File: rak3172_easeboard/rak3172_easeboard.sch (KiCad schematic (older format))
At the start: 40 parts, among them J1 Conn_Coaxial, J2 USB_C_Receptacle, SW1 SW_Push, SW2 SW_Push, U1 RAK3172, U2 FT232RL, U3 SPX3819

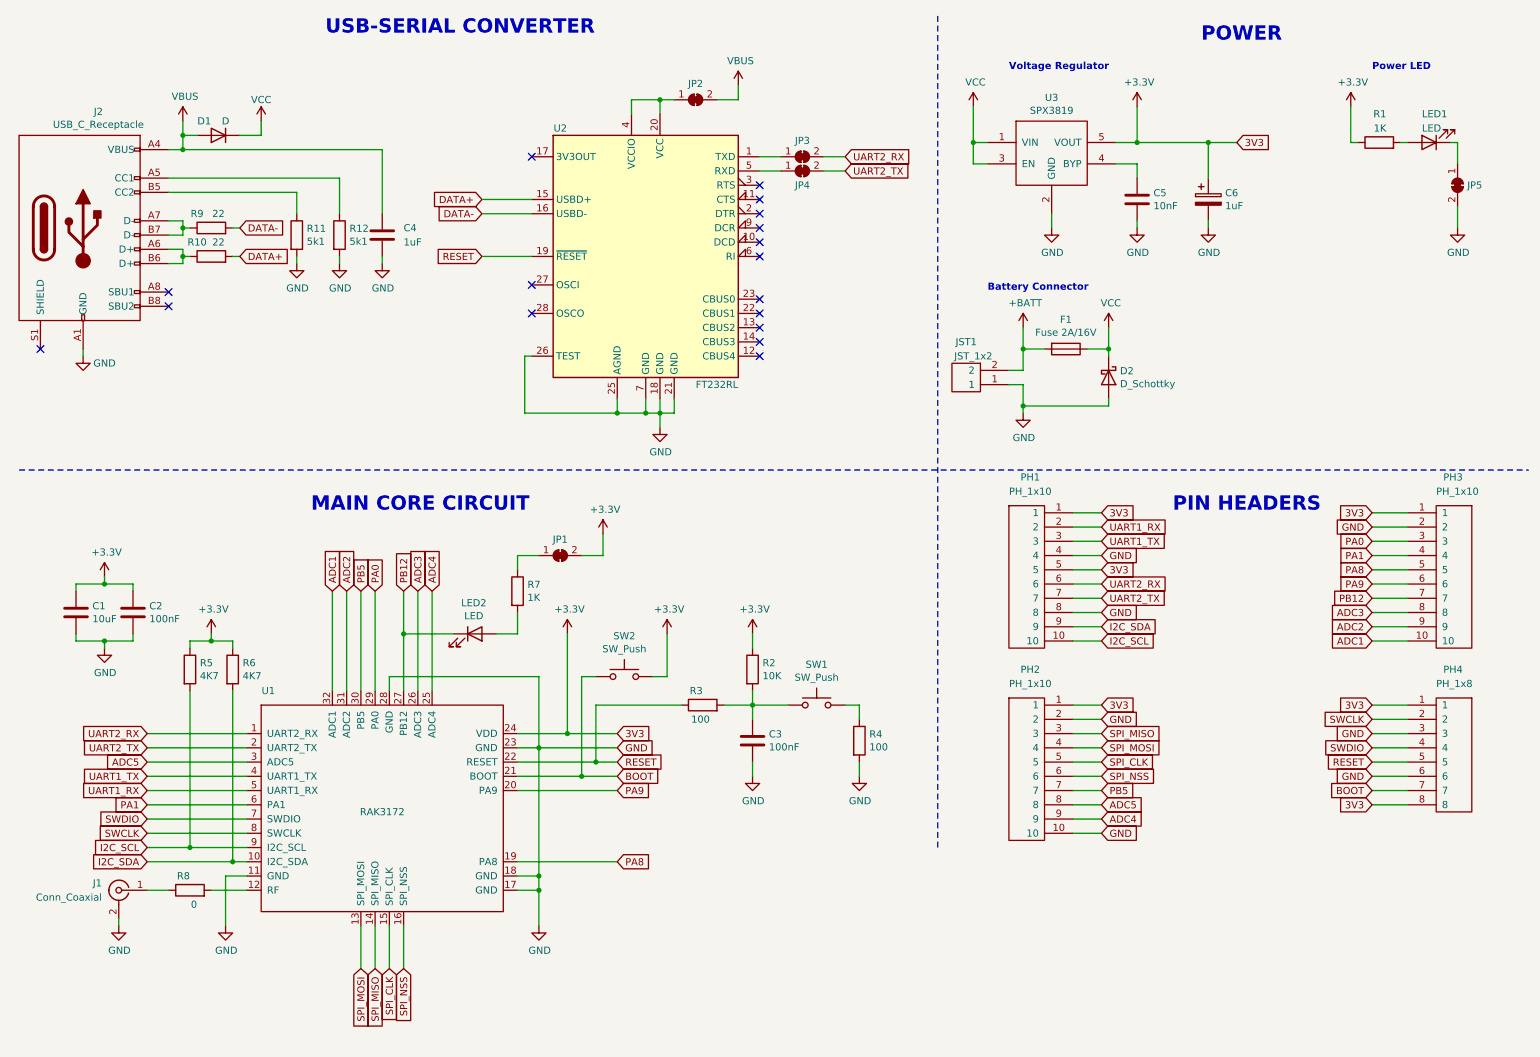
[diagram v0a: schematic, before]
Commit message: Update antenna trace. Added BOM
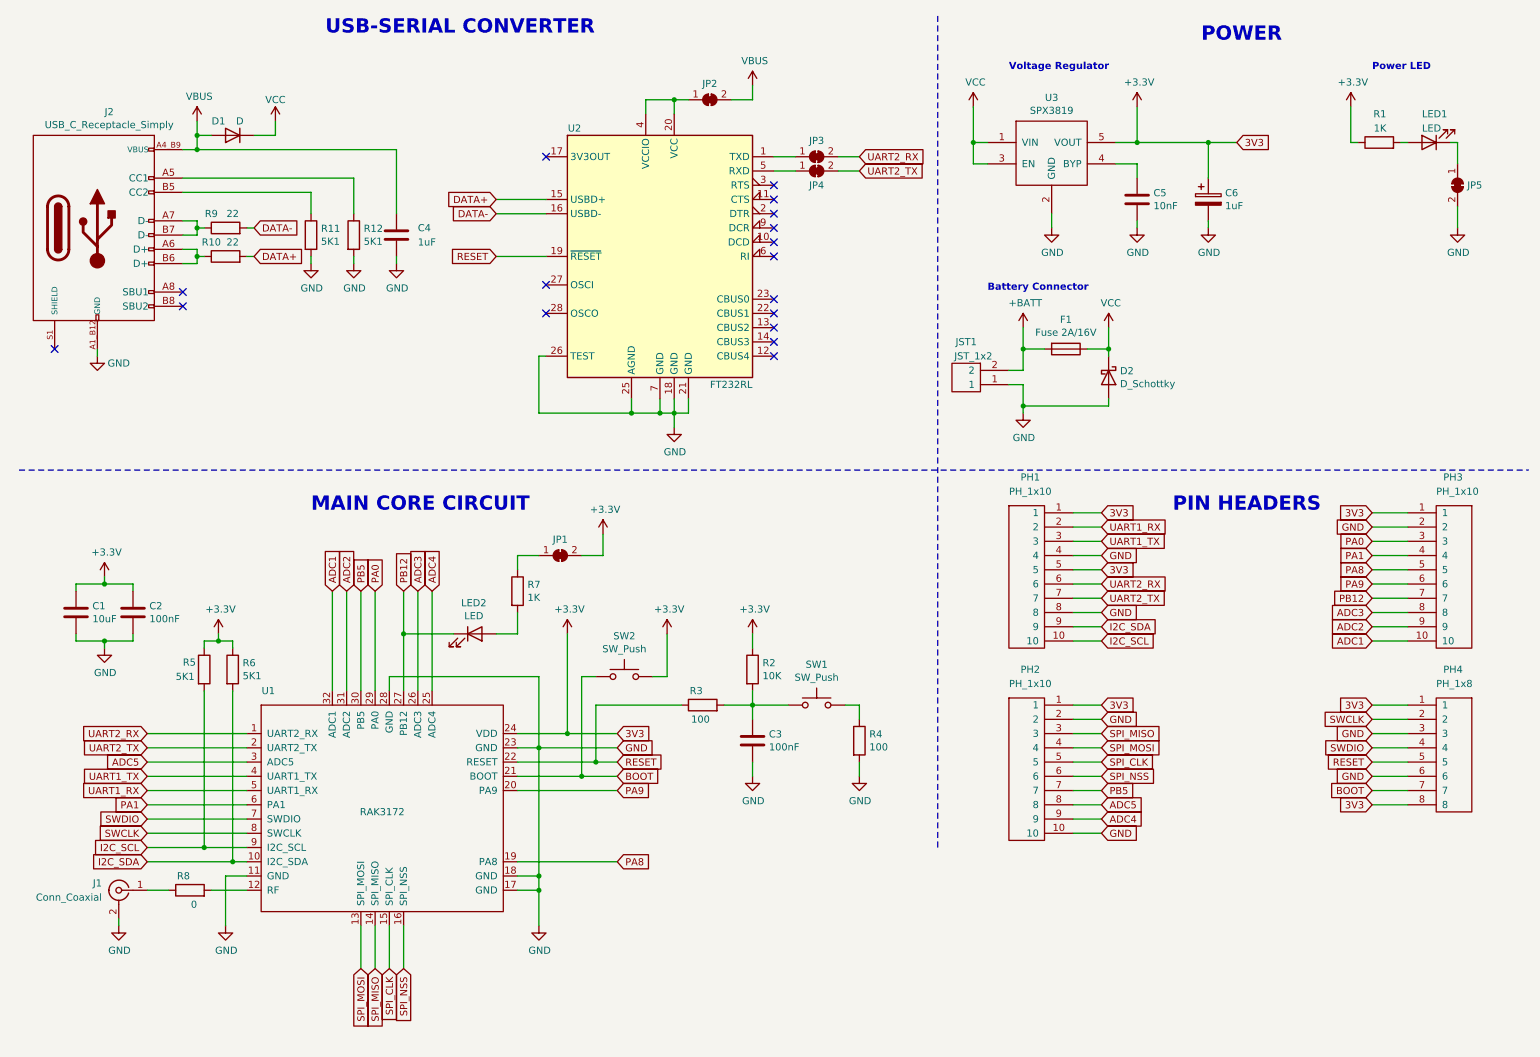
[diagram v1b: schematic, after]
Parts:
- removed J2: USB_C_Receptacle, rak3172_easeboard:USB_C_Receptacle_HRO_TYPE-C-31-M-12, symbol rak3172_easeboard:USB_C_Receptacle
- added J2: USB_C_Receptacle_Simply, rak3172_easeboard:USB_C_Receptacle_12, symbol rak3172_easeboard:USB_C_Receptacle_Simply
- C1: Last Seen Price (eur) (none) -> 0.14; Mouser (none) -> https://www.mouser.es/ProductDetail/Samsung-Electro-Mechani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
- C2, C3: Last Seen Price (eur) (none) -> 0.09; Mouser (none) -> https://www.mouser.es/ProductDetail/KEMET/C0805C104M5RACTU?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
- C4: Last Seen Price (eur) (none) -> 0.09; Mouser (none) -> https://www.mouser.es/ProductDetail/KEMET/C0805C105Z4VACTU?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
- C5: Last Seen Price (eur) (none) -> 0.09; Mouser (none) -> https://www.mouser.es/ProductDetail/KEMET/C0805C103J5RACTU?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
- C6: footprint rak3172_easeboard:C_1206_3216Metric_Pad1.33x1.80mm_HandSolder -> rak3172_easeboard:C_0805_2012Metric_Pad1.18x1.45mm_HandSolder; Last Seen Price (eur) (none) -> 0.09; Mouser (none) -> https://www.mouser.es/ProductDetail/KEMET/C0805C105Z4VACTU?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
- D1: Last Seen Price (eur) (none) -> 0.29; Mouser (none) -> https://www.mouser.es/ProductDetail/Taiwan-Semiconductor/TS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
- D2: Last Seen Price (eur) (none) -> 0.32; Mouser (none) -> https://www.mouser.es/ProductDetail/Kyocera-AVX/SD0805S020S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
- F1: Last Seen Price (eur) (none) -> 0.42; Mouser (none) -> https://www.mouser.es/ProductDetail/Littelfuse/1812L150-16D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
- JST1: Last Seen Price (eur) (none) -> 0.64; Mouser (none) -> https://www.mouser.es/ProductDetail/Adafruit/1769?qs=sGAEpi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
- LED1, LED2: Last Seen Price (eur) (none) -> 0.15; Mouser (none) -> https://www.mouser.es/ProductDetail/Wurth-Elektronik/150080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
- R1, R7: Last Seen Price (eur) (none) -> 0.09; Mouser (none) -> https://www.mouser.es/ProductDetail/Susumu/RR1220P-102-D?qs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
- R10, R9: Last Seen Price (eur) (none) -> 0.09; Mouser (none) -> https://www.mouser.es/ProductDetail/Susumu/RR1220Q-220-D?qs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
- R11, R12: value 5k1 -> 5K1; Last Seen Price (eur) (none) -> 0.09; Mouser (none) -> https://www.mouser.es/ProductDetail/Panasonic/ERA-6AED512V?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
- R2: Last Seen Price (eur) (none) -> 0.09; Mouser (none) -> https://www.mouser.es/ProductDetail/Susumu/RR1220P-103-D?qs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
- R3, R4: Last Seen Price (eur) (none) -> 0.09; Mouser (none) -> https://www.mouser.es/ProductDetail/Susumu/RR1220P-101-D?qs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
- R5, R6: value 4K7 -> 5K1; Last Seen Price (eur) (none) -> 0.09; Mouser (none) -> https://www.mouser.es/ProductDetail/Panasonic/ERA-6AED512V?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
- SW1, SW2: Last Seen Price (eur) (none) -> 0.21; Mouser (none) -> https://www.mouser.es/ProductDetail/Schurter/13019318?qs=tG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
- U1: Last Seen Price (eur) (none) -> 5.15; Mouser (none) -> https://store.rakwireless.com/products/wisduo-lpwan-module-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
- U3: Last Seen Price (eur) (none) -> 0.47; Mouser (none) -> https://www.mouser.es/ProductDetail/MaxLinear/SPX3819M5-L-3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
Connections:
- net GND: now also J2.A1_B12 (GND), J2.B1_A12 (GND)
- net VBUS: now also J2.A4_B9 (VBUS), J2.B4_A9 (VBUS)
- net at R12.1: now also J2.A5 (CC1)
- net at R10.1: now also J2.A6 (D+), J2.B6 (D+)
- net at R9.1: now also J2.A7 (D-), J2.B7 (D-)
- net at R11.1: now also J2.B5 (CC2)
- new net SHIELD: J2.S1 (SHIELD), J2.S2 (SHIELD), J2.S3 (SHIELD), J2.S4 (SHIELD)
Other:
- moved on the sheet: C4, D1, JP2, JP3, JP4, R10, R11, R12, R5, R9, U2

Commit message: UART serie protection resistors
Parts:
- added R13, R14, R15, R16: 22, rak3172_easeboard:R_0805_2012Metric_Pad1.20x1.40mm_HandSolder, symbol rak3172_easeboard:R
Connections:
- net UART1_RX: now also R16.1; no longer U1.5 (UART1_RX)
- net UART1_TX: now also R15.1; no longer U1.4 (UART1_TX)
- net UART2_RX: now also R13.1; no longer U1.1 (UART2_RX)
- net UART2_TX: now also R14.1; no longer U1.2 (UART2_TX)
- new net: R13.2, U1.1 (UART2_RX)
- new net: R14.2, U1.2 (UART2_TX)
- new net: R15.2, U1.4 (UART1_TX)
- new net: R16.2, U1.5 (UART1_RX)
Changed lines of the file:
@@
 Wire Wire Line
 	2150 6100 1450 6100
-$Comp
-L rak3172_easeboard:RAK3172 U1
-U 1 1 6153A147
-P 3100 6150
-F 0 "U1" H 2300 7000 50  0000 C CNN
-F 1 "RAK3172" H 3100 6150 50  0000 C CNN
-F 2 "rak3172_easeboard:RAK3172" H 2250 5400 50  0001 C CNN
-F 3 "https://docs.rakwireless.com/Product-Categories/WisDuo/RAK3172-Module/Datasheet" H 2300 7000 50  0001 C CNN
-F 4 "5.15" H 3100 6150 50  0001 C CNN "Last Seen Price (eur)"
-F 5 "https://store.rakwireless.com/products/wisduo-lpwan-module-rak3172?utm_source=rak3172landingpage&utm_medium=header&utm_campaign=RAKwireless&variant=40014759329990" H 3100 6150 50  0001 C CNN "Mouser"
-	1    3100 6150
-	1    0    0    -1
-$EndComp
 Wire Wire Line
 	1450 6500 2050 6500
@@
 Text GLabel 1450 6400 0    50   Input ~ 0
 I2C_SCL
-Text GLabel 1450 5900 0    50   Input ~ 0
-UART1_TX
-Text GLabel 1450 5800 0    50   Input ~ 0
-ADC5
 Text GLabel 1450 6100 0    50   Input ~ 0
 PA1
-Text GLabel 1450 6000 0    50   Input ~ 0
-UART1_RX
 Text GLabel 1450 6300 0    50   Input ~ 0
 SWCLK
@@
 	1    0    0    -1
 $EndComp
-Text GLabel 1450 5600 0    50   Input ~ 0
-UART2_RX
-Text GLabel 1450 5700 0    50   Input ~ 0
-UART2_TX
 Wire Wire Line
 	6300 1650 6450 1650
@@
 Wire Wire Line
 	5700 5400 5500 5400
-Wire Wire Line
-	2150 5600 1450 5600
-Wire Wire Line
-	1450 5700 2150 5700
-Wire Wire Line
-	2150 5800 1450 5800
-Wire Wire Line
-	1450 5900 2150 5900
-Wire Wire Line
-	2150 6000 1450 6000
+$Comp
+L rak3172_easeboard:RAK3172 U1
+U 1 1 6153A147
+P 3100 6150
+F 0 "U1" H 2300 7000 50  0000 C CNN
+F 1 "RAK3172" H 3100 6150 50  0000 C CNN
+F 2 "rak3172_easeboard:RAK3172" H 2250 5400 50  0001 C CNN
+F 3 "https://docs.rakwireless.com/Product-Categories/WisDuo/RAK3172-Module/Datasheet" H 2300 7000 50  0001 C CNN
+F 4 "5.15" H 3100 6150 50  0001 C CNN "Last Seen Price (eur)"
+F 5 "https://store.rakwireless.com/products/wisduo-lpwan-module-rak3172?utm_source=rak3172landingpage&utm_medium=header&utm_campaign=RAKwireless&variant=40014759329990" H 3100 6150 50  0001 C CNN "Mouser"
+	1    3100 6150
+	1    0    0    -1
+$EndComp
+Wire Wire Line
+	2150 6000 1800 6000
+Wire Wire Line
+	1800 5900 2150 5900
+Wire Wire Line
+	1800 5600 2150 5600
+Wire Wire Line
+	2150 5700 1800 5700
+Wire Wire Line
+	1450 5800 2150 5800
+Text GLabel 1450 5800 0    50   Input ~ 0
+ADC5
+Text GLabel 1450 5600 0    50   Input ~ 0
+UART2_RX
+Text GLabel 1450 5700 0    50   Input ~ 0
+UART2_TX
+Wire Wire Line
+	1450 5600 1500 5600
+Wire Wire Line
+	1500 5700 1450 5700
+$Comp
+L rak3172_easeboard:R R13
+U 1 1 61984AB7
+P 1650 5600
+F 0 "R13" V 1850 5700 50  0000 C CNN
+F 1 "22" V 1850 5550 50  0000 C CNN
+F 2 "rak3172_easeboard:R_0805_2012Metric_Pad1.20x1.40mm_HandSolder" V 1580 5600 50  0001 C CNN
+F 3 "https://www.mouser.es/datasheet/2/392/susumu_RR_Data_Sheet-1206438.pdf" H 1650 5600 50  0001 C CNN
+F 4 "0.09" H 1650 5600 50  0001 C CNN "Last Seen Price (eur)"
+F 5 "https://www.mouser.es/ProductDetail/Susumu/RR1220Q-220-D?qs=U7dmUkNviFsL4com4sXnaQ%3D%3D" H 1650 5600 50  0001 C CNN "Mouser"
+	1    1650 5600
+	0    -1   -1   0
+$EndComp
+$Comp
+L rak3172_easeboard:R R14
+U 1 1 61984AAF
+P 1650 5700
+F 0 "R14" V 1850 5800 50  0000 C CNN
+F 1 "22" V 1850 5650 50  0000 C CNN
+F 2 "rak3172_easeboard:R_0805_2012Metric_Pad1.20x1.40mm_HandSolder" V 1580 5700 50  0001 C CNN
+F 3 "https://www.mouser.es/datasheet/2/392/susumu_RR_Data_Sheet-1206438.pdf" H 1650 5700 50  0001 C CNN
+F 4 "0.09" H 1650 5700 50  0001 C CNN "Last Seen Price (eur)"
+F 5 "https://www.mouser.es/ProductDetail/Susumu/RR1220Q-220-D?qs=U7dmUkNviFsL4com4sXnaQ%3D%3D" H 1650 5700 50  0001 C CNN "Mouser"
+	1    1650 5700
+	0    -1   -1   0
+$EndComp
+Wire Wire Line
+	1500 5900 1450 5900
+Wire Wire Line
+	1450 6000 1500 6000
+$Comp
+L rak3172_easeboard:R R16
+U 1 1 619D2833
+P 1650 6000
+F 0 "R16" V 1650 6100 50  0000 C CNN
+F 1 "22" V 1650 5950 50  0000 C CNN
+F 2 "rak3172_easeboard:R_0805_2012Metric_Pad1.20x1.40mm_HandSolder" V 1580 6000 50  0001 C CNN
+F 3 "https://www.mouser.es/datasheet/2/392/susumu_RR_Data_Sheet-1206438.pdf" H 1650 6000 50  0001 C CNN
+F 4 "0.09" H 1650 6000 50  0001 C CNN "Last Seen Price (eur)"
+F 5 "https://www.mouser.es/ProductDetail/Susumu/RR1220Q-220-D?qs=U7dmUkNviFsL4com4sXnaQ%3D%3D" H 1650 6000 50  0001 C CNN "Mouser"
+	1    1650 6000
+	0    -1   -1   0
+$EndComp
+Text GLabel 1450 6000 0    50   Input ~ 0
+UART1_RX
+Text GLabel 1450 5900 0    50   Input ~ 0
+UART1_TX
+$Comp
+L rak3172_easeboard:R R15
+U 1 1 619D283B
+P 1650 5900
+F 0 "R15" V 1650 6000 50  0000 C CNN
+F 1 "22" V 1650 5850 50  0000 C CNN
+F 2 "rak3172_easeboard:R_0805_2012Metric_Pad1.20x1.40mm_HandSolder" V 1580 5900 50  0001 C CNN
+F 3 "https://www.mouser.es/datasheet/2/392/susumu_RR_Data_Sheet-1206438.pdf" H 1650 5900 50  0001 C CNN
+F 4 "0.09" H 1650 5900 50  0001 C CNN "Last Seen Price (eur)"
+F 5 "https://www.mouser.es/ProductDetail/Susumu/RR1220Q-220-D?qs=U7dmUkNviFsL4com4sXnaQ%3D%3D" H 1650 5900 50  0001 C CNN "Mouser"
+	1    1650 5900
+	0    -1   -1   0
+$EndComp
 $EndSCHEMATC

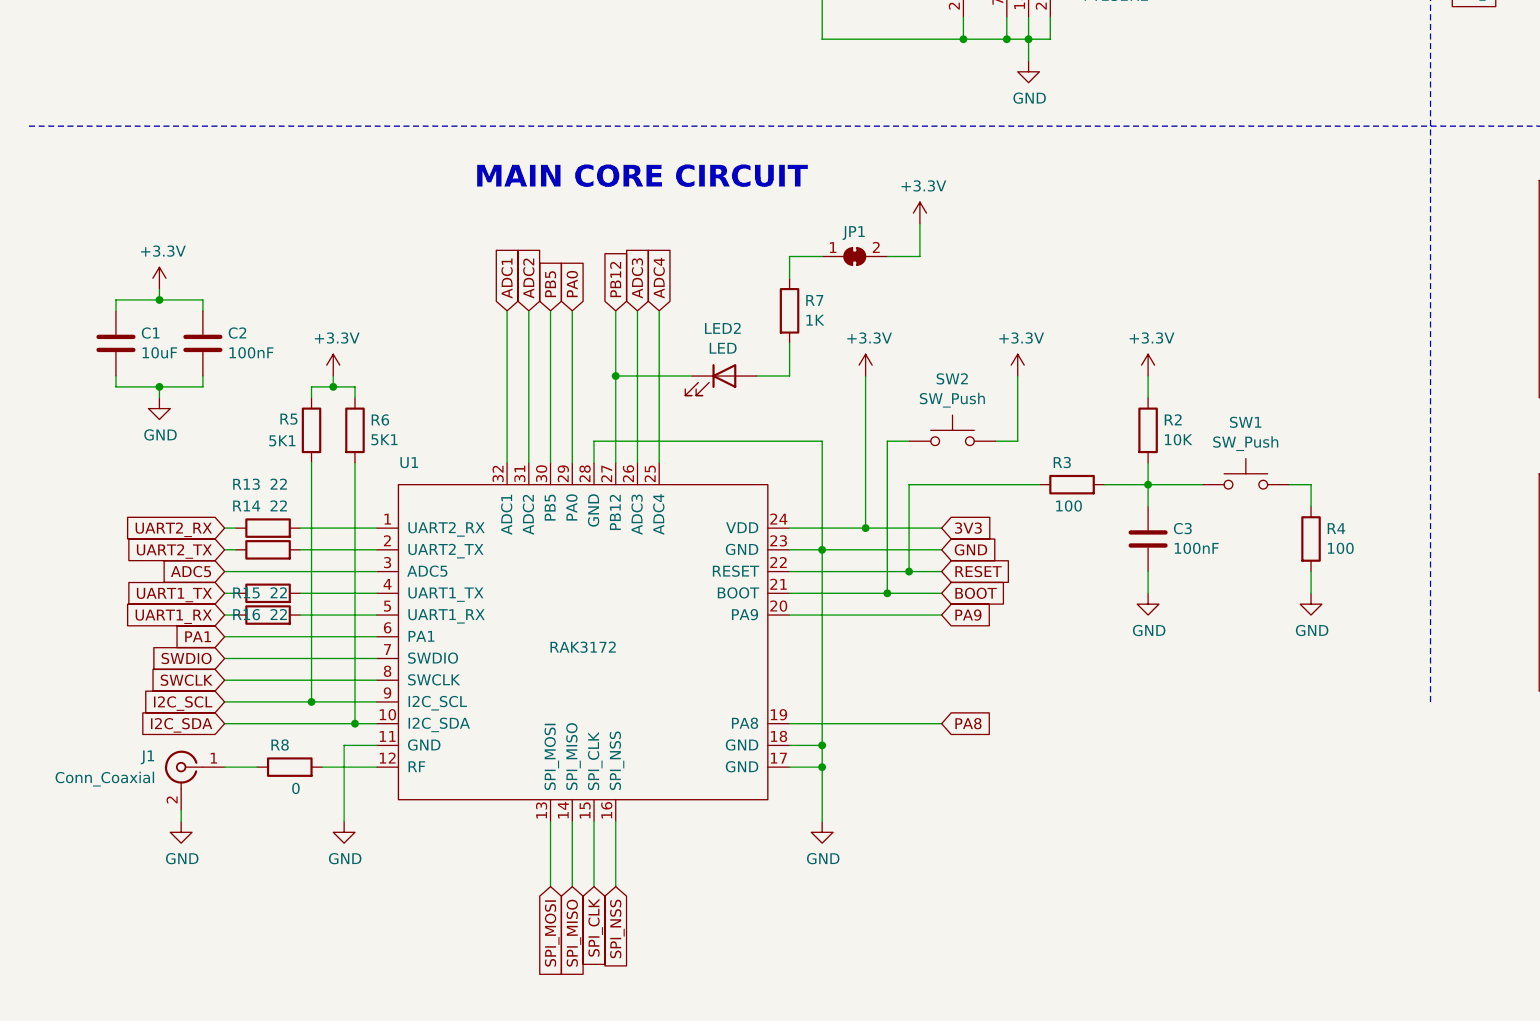
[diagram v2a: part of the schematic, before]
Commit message: Added User Button
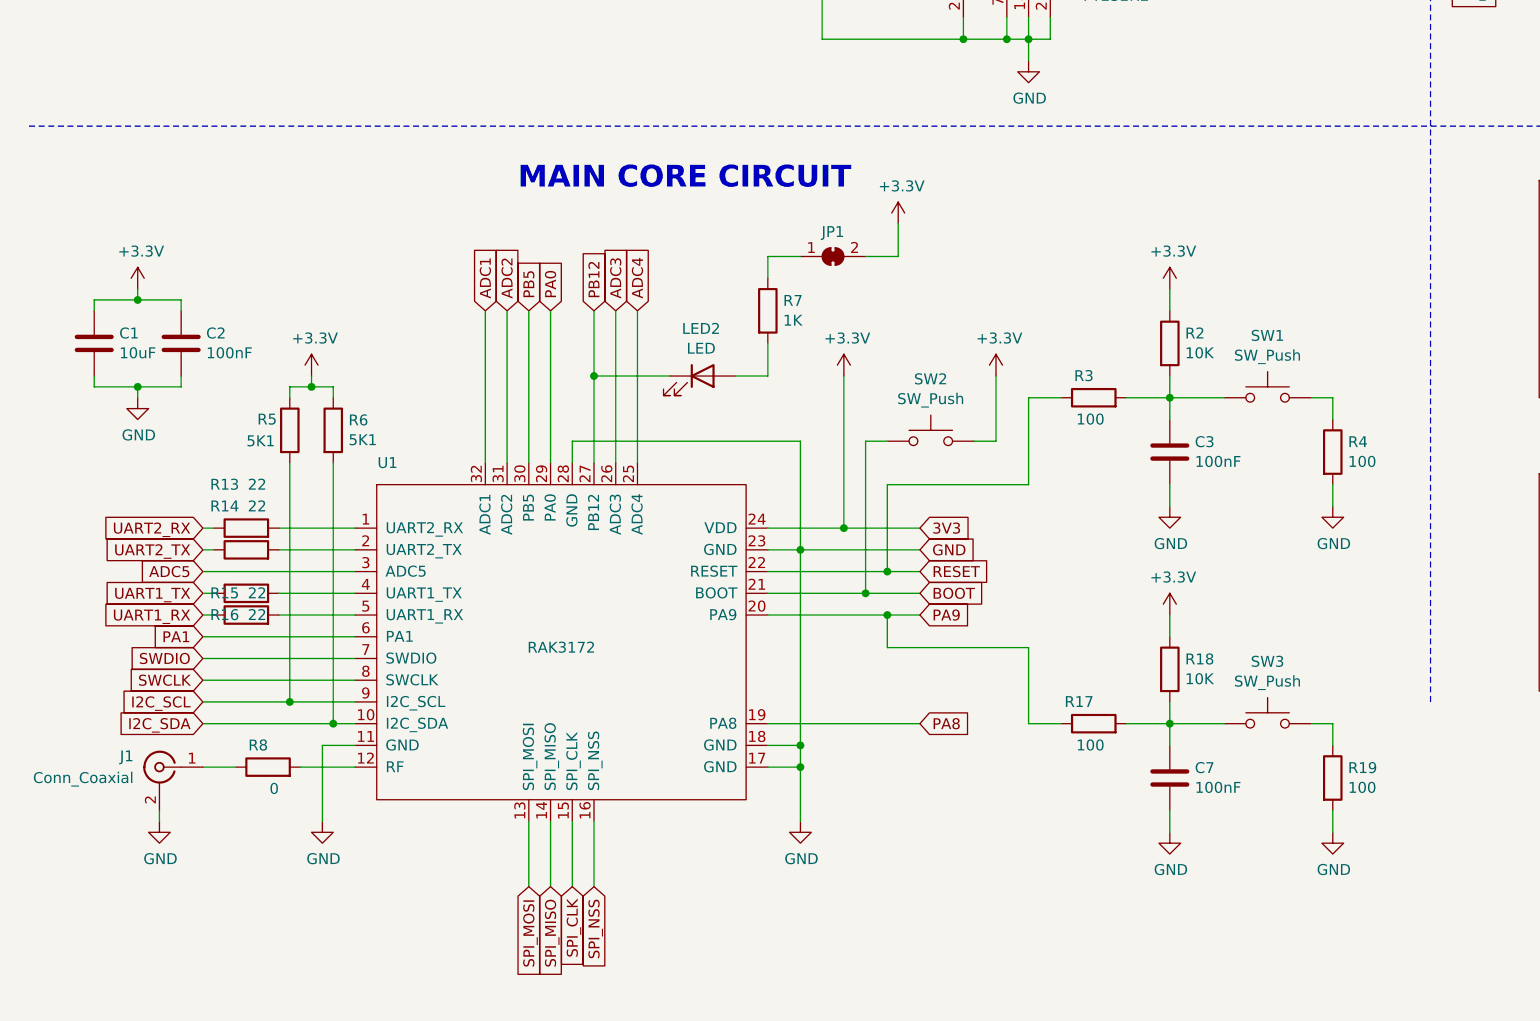
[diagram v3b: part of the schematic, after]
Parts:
- added C7: 100nF, rak3172_easeboard:C_0805_2012Metric_Pad1.18x1.45mm_HandSolder, symbol rak3172_easeboard:C
- added R17, R19: 100, rak3172_easeboard:R_0805_2012Metric_Pad1.20x1.40mm_HandSolder, symbol rak3172_easeboard:R
- added R18: 10K, rak3172_easeboard:R_0805_2012Metric_Pad1.20x1.40mm_HandSolder, symbol rak3172_easeboard:R
- added SW3: SW_Push, rak3172_easeboard:SW_Push_1P1T_NO_6x6mm_H9.5mm, symbol rak3172_easeboard:SW_Push
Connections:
- net +3V3: now also R18.1
- net GND: now also C7.2, R19.2
- net PA9: now also R17.1
- new net: C7.1, R17.2, R18.2, SW3.1
- new net: R19.1, SW3.2
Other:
- moved on the sheet: C1, C2, C3, J1, JP1, LED2, R13, R14, R15, R16, R2, R3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
